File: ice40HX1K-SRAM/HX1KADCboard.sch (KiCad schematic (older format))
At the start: 0 parts

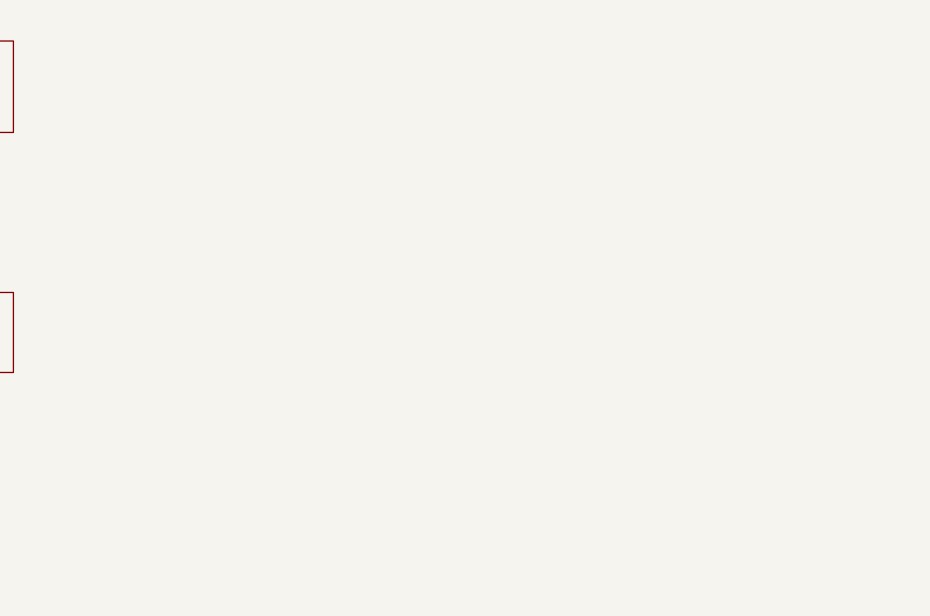
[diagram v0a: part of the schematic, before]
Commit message: Started USB => ice40 HX1K Bridge with ATSAMD11C14A
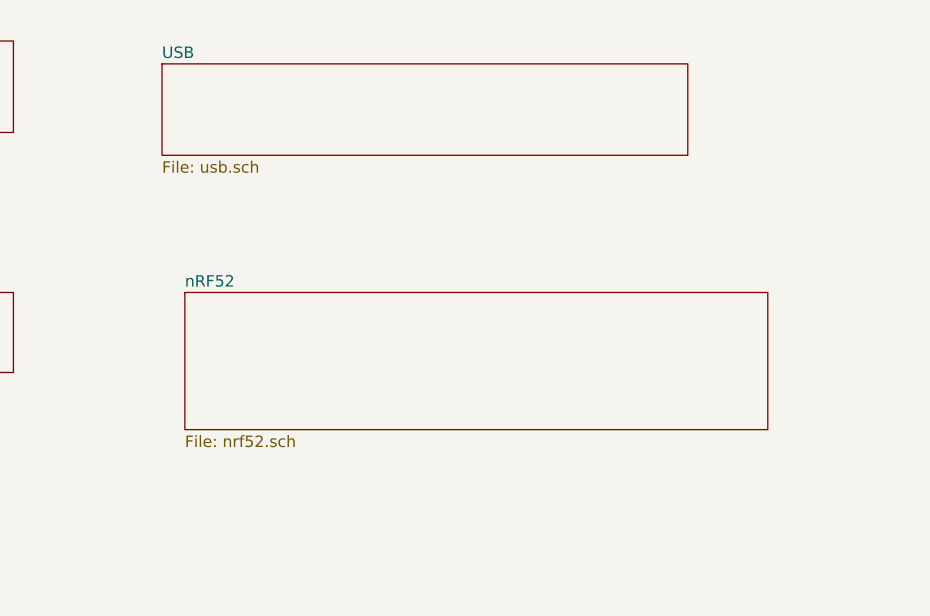
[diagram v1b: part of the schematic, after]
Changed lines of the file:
@@
 $Descr A4 11693 8268
 encoding utf-8
-Sheet 1 6
+Sheet 1 8
 Title ""
 Date ""
@@
 F1 "sram.sch" 50
 $EndSheet
+$Sheet
+S 3000 800  2300 400
+U 5E5EC834
+F0 "USB" 50
+F1 "usb.sch" 50
+$EndSheet
+$Sheet
+S 3100 1800 2550 600
+U 5E5ECC92
+F0 "nRF52" 50
+F1 "nrf52.sch" 50
+$EndSheet
 $EndSCHEMATC
